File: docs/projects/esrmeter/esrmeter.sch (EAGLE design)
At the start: 18 parts, among them IC2 TL072P

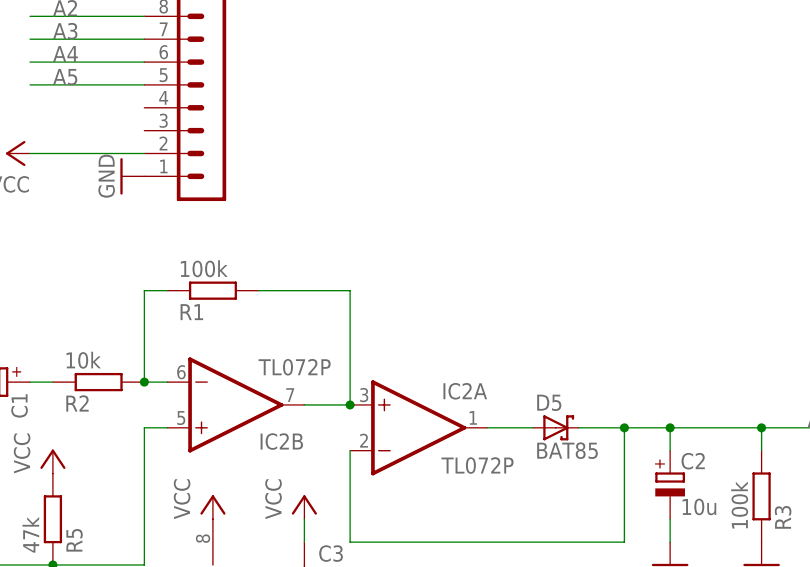
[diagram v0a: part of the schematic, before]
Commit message: esrmeter: modify schematic
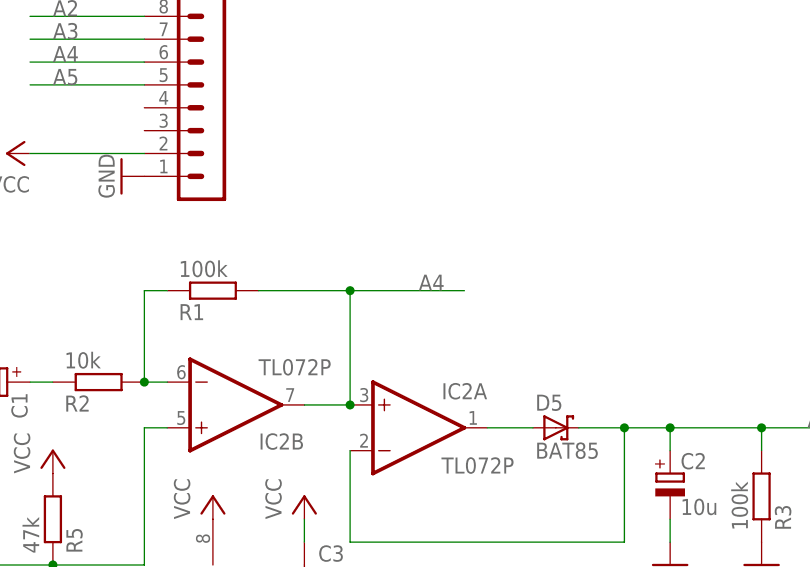
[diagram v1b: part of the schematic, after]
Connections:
- removed net N$4: IC2A.+IN, IC2B.OUT, R1.2
- net A4: now also IC2A.+IN, IC2B.OUT, R1.2
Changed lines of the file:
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@@
 <label x="213.36" y="137.16" size="1.778" layer="95"/>
 <pinref part="PC" gate="1" pin="6"/>
+<wire x1="259.08" y1="111.76" x2="246.38" y2="111.76" width="0.1524" layer="91"/>
+<label x="254" y="111.76" size="1.778" layer="95"/>
+<wire x1="241.3" y1="99.06" x2="246.38" y2="99.06" width="0.1524" layer="91"/>
+<wire x1="246.38" y1="99.06" x2="246.38" y2="111.76" width="0.1524" layer="91"/>
+<wire x1="246.38" y1="111.76" x2="236.22" y2="111.76" width="0.1524" layer="91"/>
+<junction x="246.38" y="99.06"/>
+<pinref part="IC2" gate="B" pin="OUT"/>
+<pinref part="R1" gate="G$1" pin="2"/>
+<pinref part="IC2" gate="A" pin="+IN"/>
+<junction x="246.38" y="111.76"/>
 </segment>
 </net>
@@
 </segment>
 </net>
-<net name="N$4" class="0">
-<segment>
-<wire x1="241.3" y1="99.06" x2="246.38" y2="99.06" width="0.1524" layer="91"/>
-<wire x1="246.38" y1="99.06" x2="246.38" y2="111.76" width="0.1524" layer="91"/>
-<wire x1="246.38" y1="111.76" x2="236.22" y2="111.76" width="0.1524" layer="91"/>
-<junction x="246.38" y="99.06"/>
-<pinref part="IC2" gate="B" pin="OUT"/>
-<pinref part="R1" gate="G$1" pin="2"/>
-<pinref part="IC2" gate="A" pin="+IN"/>
-</segment>
-</net>
